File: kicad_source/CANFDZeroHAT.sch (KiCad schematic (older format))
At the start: 24 parts, among them CN1 RASPI-IO, CN2 CONN_01X04, CN3 GH_SM04B-GHS-TB, CN4 GH_SM04B-GHS-TB, SW1 JS202011JCQN, U1 MCP2517FD, U2 SN65HVD232, Y1 RH100-20.000-20-3030-TR

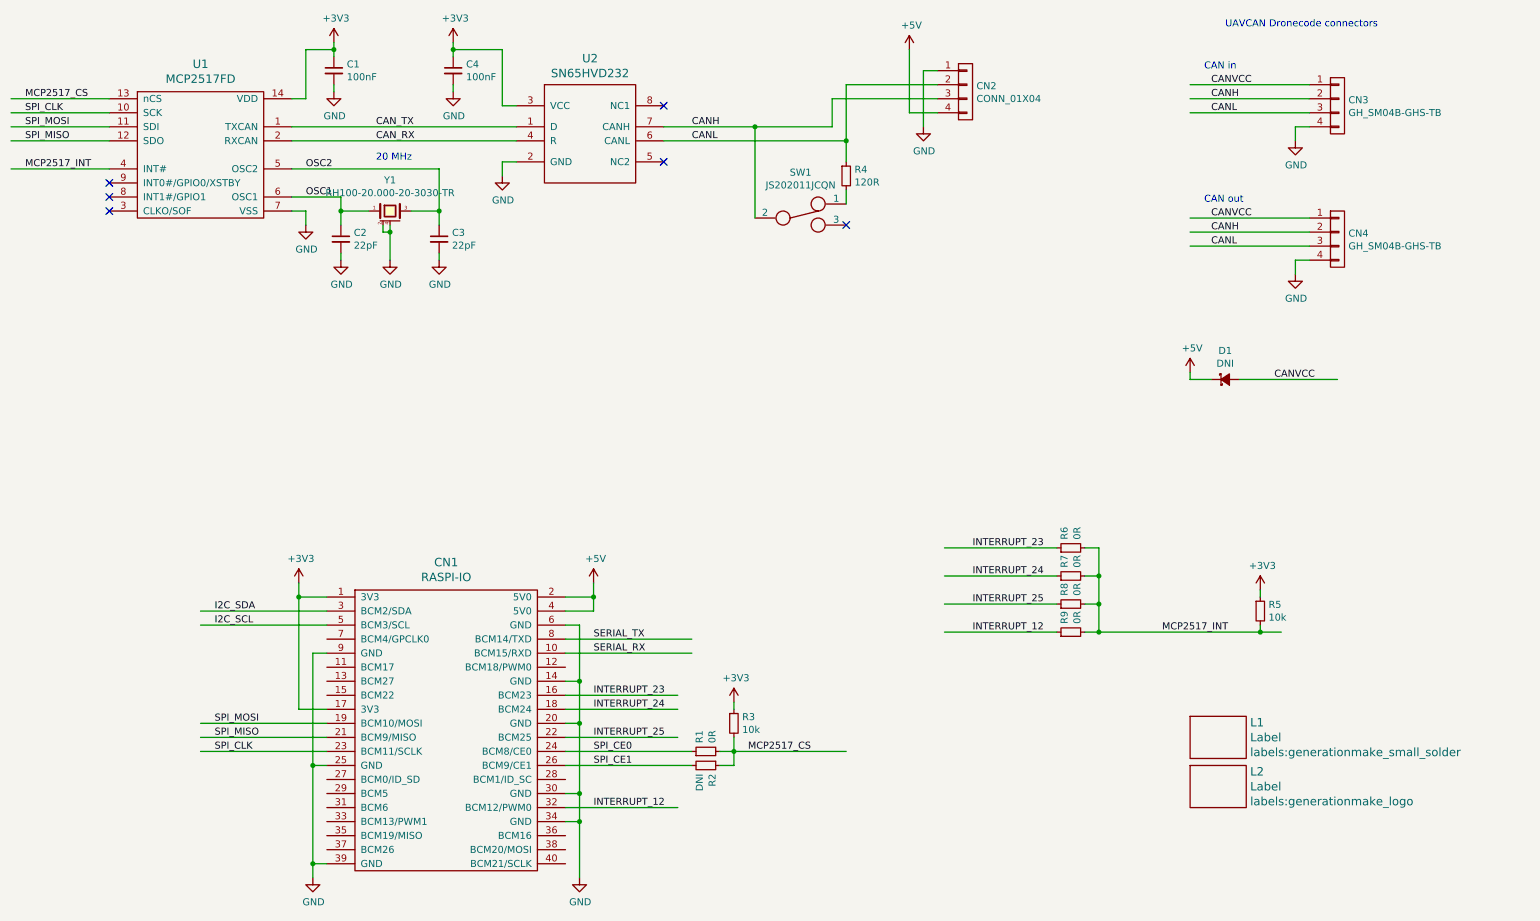
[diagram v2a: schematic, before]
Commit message: updated some part numbers
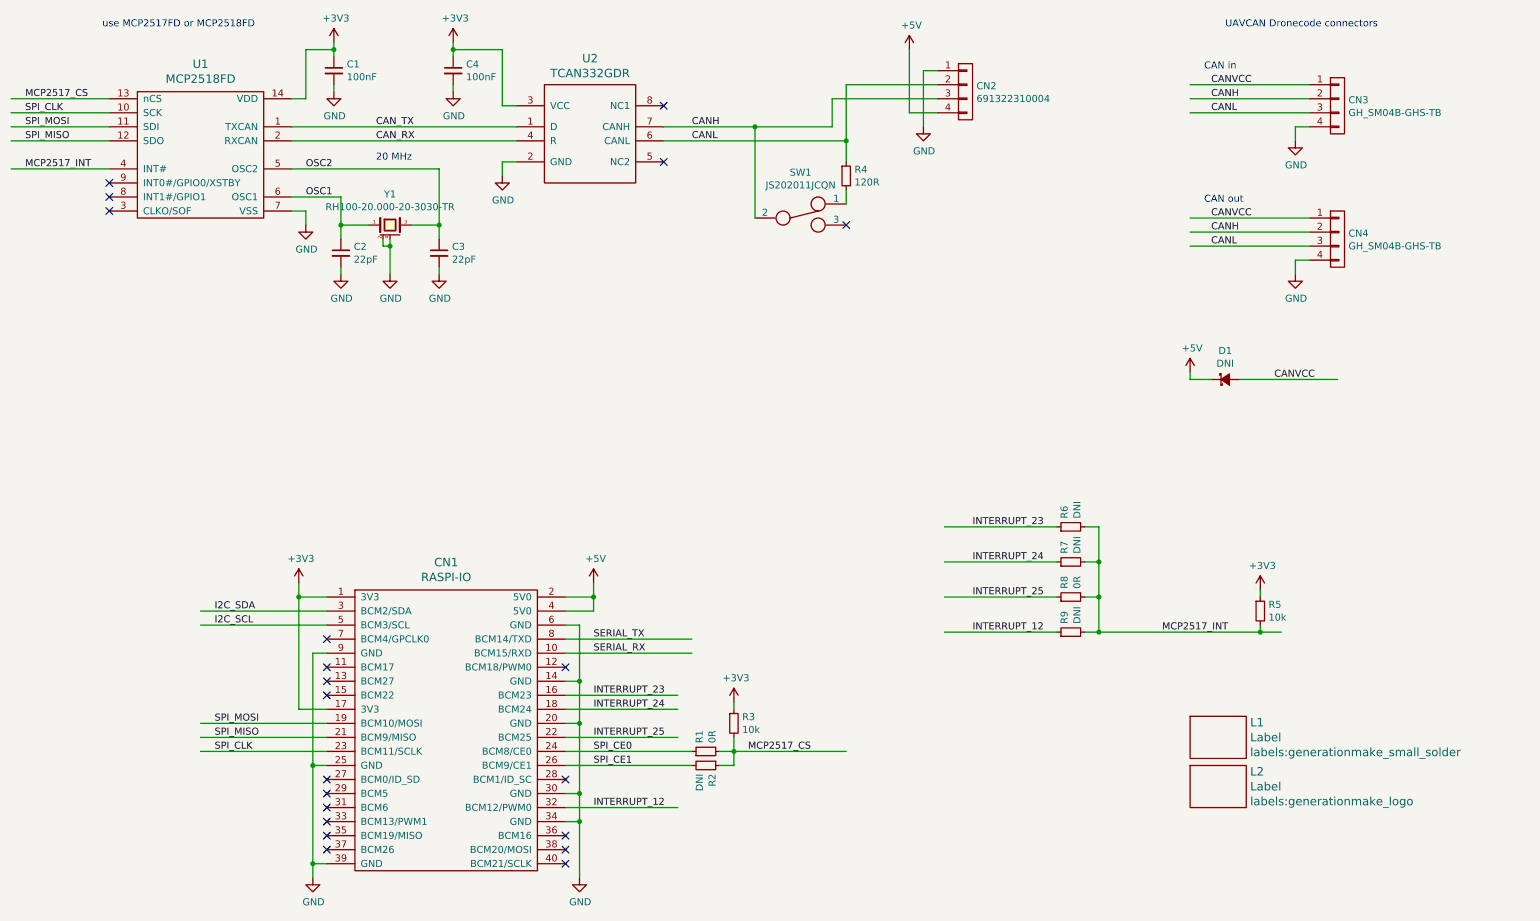
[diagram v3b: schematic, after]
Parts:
- CN2: value CONN_01X04 -> 691322310004; footprint CON_wuerth:WR-TBL_691210910004 -> CON_wuerth:WR-TBL_691322310004
- R6, R7, R9: value 0R -> DNI
- U1: value MCP2517FD -> MCP2518FD
- U2: value SN65HVD232 -> TCAN332GDR
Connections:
- no-connect marks 6 -> 21
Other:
- note added: "use MCP2517FD or MCP2518FD"
- moved on the sheet: C2, C3, R6, R7, R8, Y1
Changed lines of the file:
@@
 AR Path="/5FD7518E" Ref="U1"  Part="1"
 F 0 "U1" H 2000 2447 60  0000 C CNN
-F 1 "MCP2517FD" H 2000 2341 60  0000 C CNN
+F 1 "MCP2518FD" H 2000 2341 60  0000 C CNN
 F 2 "SOIC:SOIC-14_3.9x8.7mm_Pitch1.27mm" H 2000 2341 60  0001 C CNN
 F 3 "" H 2000 1800 60  0000 C CNN
@@
 L devices:Crystal_SMD_4Pad Y?
 U 1 1 5FD751A0
-P 3350 2200
+P 3350 2300
 AR Path="/5FD58A5B/5FD751A0" Ref="Y?"  Part="1"
 AR Path="/5FD751A0" Ref="Y1"  Part="1"
-F 0 "Y1" H 3350 2420 50  0000 C CNN
-F 1 "RH100-20.000-20-3030-TR" H 3350 2329 50  0000 C CNN
-F 2 "crystals:Crystal_SMD_3.2x2.5mm_4Pad" H 3350 2000 50  0001 C CNN
-F 3 "" H 3350 2200 50  0000 C CNN
-	1    3350 2200
+F 0 "Y1" H 3350 2520 50  0000 C CNN
+F 1 "RH100-20.000-20-3030-TR" H 3350 2429 50  0000 C CNN
+F 2 "crystals:Crystal_SMD_3.2x2.5mm_4Pad" H 3350 2100 50  0001 C CNN
+F 3 "" H 3350 2300 50  0000 C CNN
+	1    3350 2300
 	1    0    0    -1
 $EndComp
@@
 L devices:C_0603 C?
 U 1 1 5FD751B2
-P 3000 2400
+P 3000 2500
 AR Path="/5FD58A5B/5FD751B2" Ref="C?"  Part="1"
 AR Path="/5FD751B2" Ref="C2"  Part="1"
-F 0 "C2" H 3092 2446 50  0000 L CNN
-F 1 "22pF" H 3092 2355 50  0000 L CNN
-F 2 "capacitors:C_0603" H 3000 2250 50  0001 C CNN
-F 3 "" H 3000 2400 50  0000 C CNN
-	1    3000 2400
+F 0 "C2" H 3092 2546 50  0000 L CNN
+F 1 "22pF" H 3092 2455 50  0000 L CNN
+F 2 "capacitors:C_0603" H 3000 2350 50  0001 C CNN
+F 3 "" H 3000 2500 50  0000 C CNN
+	1    3000 2500
 	1    0    0    -1
 $EndComp
@@
 L devices:C_0603 C?
 U 1 1 5FD751B8
-P 3700 2400
+P 3700 2500
 AR Path="/5FD58A5B/5FD751B8" Ref="C?"  Part="1"
 AR Path="/5FD751B8" Ref="C3"  Part="1"
-F 0 "C3" H 3792 2446 50  0000 L CNN
-F 1 "22pF" H 3792 2355 50  0000 L CNN
-F 2 "capacitors:C_0603" H 3700 2250 50  0001 C CNN
-F 3 "" H 3700 2400 50  0000 C CNN
-	1    3700 2400
+F 0 "C3" H 3792 2546 50  0000 L CNN
+F 1 "22pF" H 3792 2455 50  0000 L CNN
+F 2 "capacitors:C_0603" H 3700 2350 50  0001 C CNN
+F 3 "" H 3700 2500 50  0000 C CNN
+	1    3700 2500
 	1    0    0    -1
 $EndComp
@@
 L power-supply:GND #PWR?
 U 1 1 5FD751BE
-P 3000 2550
+P 3000 2650
 AR Path="/5FD58A5B/5FD751BE" Ref="#PWR?"  Part="1"
 AR Path="/5FD751BE" Ref="#PWR04"  Part="1"
-F 0 "#PWR04" H 3000 2300 50  0001 C CNN
-F 1 "GND" H 3005 2377 50  0000 C CNN
-F 2 "" H 3000 2550 50  0000 C CNN
-F 3 "" H 3000 2550 50  0000 C CNN
-	1    3000 2550
+F 0 "#PWR04" H 3000 2400 50  0001 C CNN
+F 1 "GND" H 3005 2477 50  0000 C CNN
+F 2 "" H 3000 2650 50  0000 C CNN
+F 3 "" H 3000 2650 50  0000 C CNN
+	1    3000 2650
 	1    0    0    -1
 $EndComp
@@
 L power-supply:GND #PWR?
 U 1 1 5FD751C4
-P 3350 2550
+P 3350 2650
 AR Path="/5FD58A5B/5FD751C4" Ref="#PWR?"  Part="1"
 AR Path="/5FD751C4" Ref="#PWR05"  Part="1"
-F 0 "#PWR05" H 3350 2300 50  0001 C CNN
-F 1 "GND" H 3355 2377 50  0000 C CNN
-F 2 "" H 3350 2550 50  0000 C CNN
-F 3 "" H 3350 2550 50  0000 C CNN
-	1    3350 2550
+F 0 "#PWR05" H 3350 2400 50  0001 C CNN
+F 1 "GND" H 3355 2477 50  0000 C CNN
+F 2 "" H 3350 2650 50  0000 C CNN
+F 3 "" H 3350 2650 50  0000 C CNN
+	1    3350 2650
 	1    0    0    -1
 $EndComp
@@
 L power-supply:GND #PWR?
 U 1 1 5FD751CA
-P 3700 2550
+P 3700 2650
 AR Path="/5FD58A5B/5FD751CA" Ref="#PWR?"  Part="1"
 AR Path="/5FD751CA" Ref="#PWR06"  Part="1"
-F 0 "#PWR06" H 3700 2300 50  0001 C CNN
-F 1 "GND" H 3705 2377 50  0000 C CNN
-F 2 "" H 3700 2550 50  0000 C CNN
-F 3 "" H 3700 2550 50  0000 C CNN
-	1    3700 2550
+F 0 "#PWR06" H 3700 2400 50  0001 C CNN
+F 1 "GND" H 3705 2477 50  0000 C CNN
+F 2 "" H 3700 2650 50  0000 C CNN
+F 3 "" H 3700 2650 50  0000 C CNN
+	1    3700 2650
 	1    0    0    -1
 $EndComp
@@
 	2650 1900 3700 1900
 Wire Wire Line
-	3700 1900 3700 2200
-Wire Wire Line
 	2650 2100 3000 2100
-Wire Wire Line
-	3000 2100 3000 2200
 Wire Wire Line
 	2650 2200 2750 2200
@@
 	2950 1300 2950 1350
 Wire Wire Line
-	3000 2500 3000 2550
-Wire Wire Line
-	3350 2300 3350 2350
-Wire Wire Line
-	3700 2500 3700 2550
-Wire Wire Line
-	3300 2300 3300 2350
-Wire Wire Line
-	3300 2350 3350 2350
-Connection ~ 3350 2350
-Wire Wire Line
-	3350 2350 3350 2550
-Wire Wire Line
-	3500 2200 3700 2200
-Connection ~ 3700 2200
-Wire Wire Line
-	3700 2200 3700 2300
-Wire Wire Line
-	3200 2200 3000 2200
-Connection ~ 3000 2200
-Wire Wire Line
-	3000 2200 3000 2300
+	3000 2600 3000 2650
+Wire Wire Line
+	3350 2400 3350 2450
+Wire Wire Line
+	3700 2600 3700 2650
+Wire Wire Line
+	3300 2400 3300 2450
+Wire Wire Line
+	3300 2450 3350 2450
+Connection ~ 3350 2450
+Wire Wire Line
+	3350 2450 3350 2650
+Wire Wire Line
+	3500 2300 3700 2300
+Connection ~ 3700 2300
+Wire Wire Line
+	3700 2300 3700 2400
+Wire Wire Line
+	3200 2300 3000 2300
+Connection ~ 3000 2300
+Wire Wire Line
+	3000 2300 3000 2400
 Text Label 2750 1900 0    50   ~ 0
 OSC2
@@
 AR Path="/5FD751FF" Ref="U2"  Part="1"
 F 0 "U2" H 4775 2887 60  0000 C CNN
-F 1 "SN65HVD232" H 4775 2781 60  0000 C CNN
+F 1 "TCAN332GDR" H 4775 2781 60  0000 C CNN
 F 2 "SOIC:SOIJ-8_5.3x5.3mm_Pitch1.27mm" H 5100 1950 60  0001 C CNN
 F 3 "" H 4250 2150 60  0000 C CNN
@@
 AR Path="/5FD75207" Ref="CN2"  Part="1"
 F 0 "CN2" H 7528 1391 50  0000 L CNN
-F 1 "CONN_01X04" H 7528 1300 50  0000 L CNN
-F 2 "CON_wuerth:WR-TBL_691210910004" H 7450 1350 50  0001 C CNN
+F 1 "691322310004" H 7528 1300 50  0000 L CNN
+F 2 "CON_wuerth:WR-TBL_691322310004" H 7450 1350 50  0001 C CNN
 F 3 "" H 7450 1350 50  0000 C CNN
 	1    7450 1350
@@
 INTERRUPT_12
 Wire Wire Line
-	7300 5000 8100 5000
-Text Label 7500 5000 0    50   ~ 0
+	7300 4950 8100 4950
+Text Label 7500 4950 0    50   ~ 0
 INTERRUPT_25
 Wire Wire Line
-	7300 4800 8100 4800
-Text Label 7500 4800 0    50   ~ 0
+	7300 4700 8100 4700
+Text Label 7500 4700 0    50   ~ 0
 INTERRUPT_24
 Wire Wire Line
-	7300 4600 8100 4600
-Text Label 7500 4600 0    50   ~ 0
+	7300 4450 8100 4450
+Text Label 7500 4450 0    50   ~ 0
 INTERRUPT_23
 Wire Wire Line
@@
 AR Path="/5FDE9CB4" Ref="R9"  Part="1"
 F 0 "R9" H 8259 5246 50  0000 L CNN
-F 1 "0R" H 8259 5155 50  0000 L CNN
+F 1 "DNI" H 8259 5155 50  0000 L CNN
 F 2 "resistors:R_0603" H 8200 5050 50  0001 C CNN
 F 3 "" H 8200 5200 50  0000 C CNN
@@
 L devices:R_0603 R?
 U 1 1 5FDEA10B
-P 8200 5000
+P 8200 4950
 AR Path="/5FD58A5B/5FDEA10B" Ref="R?"  Part="1"
 AR Path="/5FDEA10B" Ref="R8"  Part="1"
-F 0 "R8" H 8259 5046 50  0000 L CNN
-F 1 "0R" H 8259 4955 50  0000 L CNN
-F 2 "resistors:R_0603" H 8200 4850 50  0001 C CNN
-F 3 "" H 8200 5000 50  0000 C CNN
-	1    8200 5000
+F 0 "R8" H 8259 4996 50  0000 L CNN
+F 1 "0R" H 8259 4905 50  0000 L CNN
+F 2 "resistors:R_0603" H 8200 4800 50  0001 C CNN
+F 3 "" H 8200 4950 50  0000 C CNN
+	1    8200 4950
 	0    -1   -1   0
 $EndComp
@@
 L devices:R_0603 R?
 U 1 1 5FDEA376
-P 8200 4800
+P 8200 4700
 AR Path="/5FD58A5B/5FDEA376" Ref="R?"  Part="1"
 AR Path="/5FDEA376" Ref="R7"  Part="1"
-F 0 "R7" H 8259 4846 50  0000 L CNN
-F 1 "0R" H 8259 4755 50  0000 L CNN
-F 2 "resistors:R_0603" H 8200 4650 50  0001 C CNN
-F 3 "" H 8200 4800 50  0000 C CNN
-	1    8200 4800
+F 0 "R7" H 8259 4746 50  0000 L CNN
+F 1 "DNI" H 8259 4655 50  0000 L CNN
+F 2 "resistors:R_0603" H 8200 4550 50  0001 C CNN
+F 3 "" H 8200 4700 50  0000 C CNN
+	1    8200 4700
 	0    -1   -1   0
 $EndComp
@@
 L devices:R_0603 R?
 U 1 1 5FDEE754
-P 8200 4600
+P 8200 4450
 AR Path="/5FD58A5B/5FDEE754" Ref="R?"  Part="1"
 AR Path="/5FDEE754" Ref="R6"  Part="1"
-F 0 "R6" H 8259 4646 50  0000 L CNN
-F 1 "0R" H 8259 4555 50  0000 L CNN
-F 2 "resistors:R_0603" H 8200 4450 50  0001 C CNN
-F 3 "" H 8200 4600 50  0000 C CNN
-	1    8200 4600
+F 0 "R6" H 8259 4496 50  0000 L CNN
+F 1 "DNI" H 8259 4405 50  0000 L CNN
+F 2 "resistors:R_0603" H 8200 4300 50  0001 C CNN
+F 3 "" H 8200 4450 50  0000 C CNN
+	1    8200 4450
 	0    -1   -1   0
 $EndComp
-Wire Wire Line
-	8300 4600 8400 4600
-Wire Wire Line
-	8400 4600 8400 4800
 Connection ~ 8400 5200
 Wire Wire Line
 	8400 5200 9550 5200
-Wire Wire Line
-	8300 5000 8400 5000
-Connection ~ 8400 5000
-Wire Wire Line
-	8400 5000 8400 5200
-Wire Wire Line
-	8300 4800 8400 4800
-Connection ~ 8400 4800
-Wire Wire Line
-	8400 4800 8400 5000
+Text Notes 1300 900  0    50   ~ 0
+use MCP2517FD or MCP2518FD
+Wire Wire Line
+	8300 4450 8400 4450
+Wire Wire Line
+	8300 4700 8400 4700
+Connection ~ 8400 4700
+Wire Wire Line
+	8300 4950 8400 4950
+Connection ~ 8400 4950
+Wire Wire Line
+	8400 4950 8400 5200
+Wire Wire Line
+	8400 4700 8400 4950
+Wire Wire Line
+	8400 4450 8400 4700
+NoConn ~ 4600 6850
+NoConn ~ 4600 6750
+NoConn ~ 4600 6650
+NoConn ~ 4600 6250
+NoConn ~ 4600 5450
+NoConn ~ 2900 5250
+NoConn ~ 2900 5450
+NoConn ~ 2900 5550
+NoConn ~ 2900 5650
+NoConn ~ 2900 6250
+NoConn ~ 2900 6350
+NoConn ~ 2900 6450
+NoConn ~ 2900 6550
+NoConn ~ 2900 6650
+NoConn ~ 2900 6750
+Wire Wire Line
+	3700 1900 3700 2300
+Wire Wire Line
+	3000 2100 3000 2300
 $EndSCHEMATC
